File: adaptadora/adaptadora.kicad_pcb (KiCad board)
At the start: 2 copper layers, 193 x 100 mm, 106 parts, among them J1 Conn_Coaxial, J10 Conn_Coaxial, J11 Conn_Coaxial, J12 Conn_Coaxial, J13 Conn_Coaxial, J14 Conn_Coaxial, J15 Conn_Coaxial, J16 Conn_Coaxial, J17 Conn_Coaxial, J18 Conn_Coaxial, J19 Conn_Coaxial, J2 Conn_Coaxial, J20 Conn_Coaxial, J22 Conn_Coaxial, J3 Conn_Coaxial, J4 Conn_Coaxial, J5 Conn_02x20_Odd_Even, J6 Conn_01x02, J7 Conn_02x20_Odd_Even, J8 Conn_01x04, J9 Conn_01x02, U11 LM361MX_NOPB, U12 LM361MX_NOPB, U13 LM361MX_NOPB, U14 LM361MX_NOPB, U21 TLV2772IDR, U22 TLV2772IDR, U23 TLV2772IDR, U25 TLV2772IDR, U31 SN74LVC2T45DCUR, U32 SN74LVC2T45DCUR

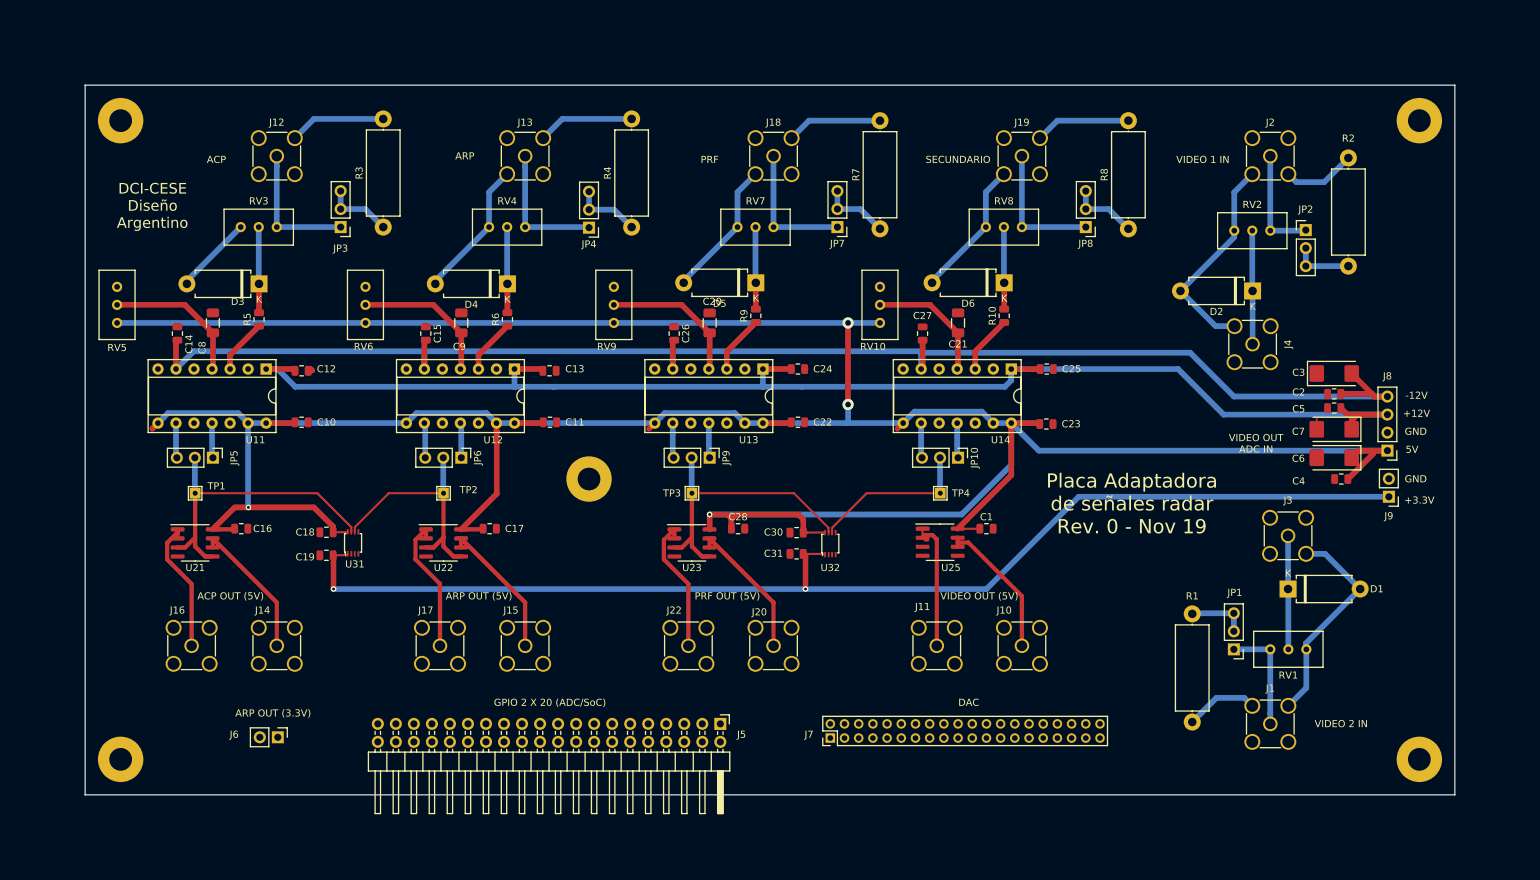
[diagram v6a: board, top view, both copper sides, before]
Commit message: se agrega planos de tierra
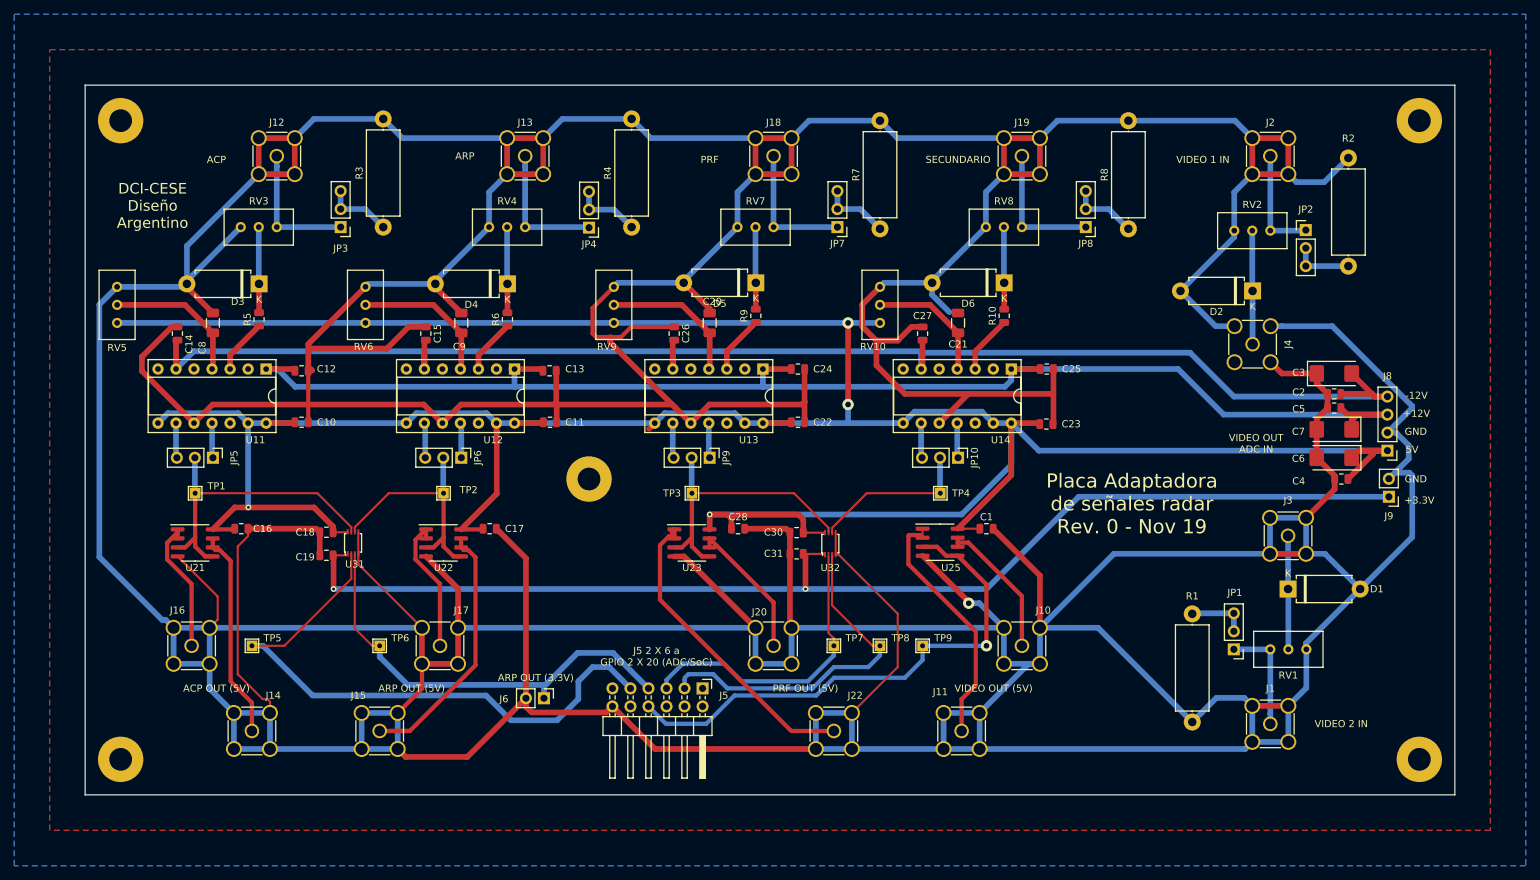
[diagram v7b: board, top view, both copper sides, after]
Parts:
- removed J7: Conn_02x20_Odd_Even, Connector_PinHeader_2.00mm:PinHeader_2x20_P2.00mm_Vertical
- added TP5: TestPoint, adaptadora:TestPoint_THTPad_1.5x1.5mm_Drill0.7mm, F.Cu at (67.5, 124.0)
- added TP6: TestPoint, adaptadora:TestPoint_THTPad_1.5x1.5mm_Drill0.7mm, F.Cu at (85.5, 124.0)
- added TP7: TestPoint, adaptadora:TestPoint_THTPad_1.5x1.5mm_Drill0.7mm, F.Cu at (149.5, 124.0)
- added TP8: TestPoint, adaptadora:TestPoint_THTPad_1.5x1.5mm_Drill0.7mm, F.Cu at (156.0, 124.0)
- added TP9: TestPoint, adaptadora:TestPoint_THTPad_1.5x1.5mm_Drill0.7mm, F.Cu at (162.0, 124.0)
- J5: value Conn_02x20_Odd_Even -> Conn_02x06_Odd_Even; footprint Connector_PinHeader_2.54mm:PinHeader_2x20_P2.54mm_Horizontal -> Connector_PinHeader_2.54mm:PinHeader_2x06_P2.54mm_Horizontal
- R10, R5, R6, R9: value 100-1/8W-5% -> 100 - 1/8W - 5%
- moved J6 37.9 mm to (108.7, 131.4)
- moved J15 23.8 mm to (85.5, 136.0)
- moved J22 23.8 mm to (149.5, 136.0)
- moved J11 12.5 mm to (167.5, 136.0)
- moved J14 12.5 mm to (67.5, 136.0)
- moved J5 5.59 mm to (131.0, 130.0)
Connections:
- J5 pad 1: /ACP_3P3 -> Net-(J5-Pad1)
- J5 pad 2: /VIDEO_DIGITAL -> Net-(J5-Pad2)
- J5 pad 3: /ACP_3P3 -> /V_COMP_3P3
- J5 pad 4: DAC_CLK -> Net-(J5-Pad4)
- J5 pad 7: /V_COMP_3P3 -> /ARP_3P3
- J5 pad 8: Net-(J5-Pad8) -> /VIDEO_DIGITAL
- J5 pad 9: Net-(J5-Pad9) -> /ACP_3P3
- J6 pad 1: /ACP_3P3 -> /ARP_3P3
- U31 pad 3: /ACP_3P3 -> /ARP_3P3
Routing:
- net GND: track 207.9 -> 1592.2 mm, vias 0 -> 1
- net /ACP_3P3: track 0.00 -> 84.9 mm
- net /VIDEO_DIGITAL: track 0.00 -> 74.2 mm, vias 0 -> 1
- net /ARP_3P3: track 0.00 -> 61.9 mm
- net /V_COMP_3P3: track 0.00 -> 50.3 mm
- net /PRF_3P3: track 0.00 -> 42.4 mm
- net Net-(J22-Pad1): track 19.7 -> 44.2 mm
- net Net-(J15-Pad1): track 20.1 -> 38.9 mm
- net Net-(J11-Pad1): track 19.6 -> 35.7 mm
- net Net-(J14-Pad1): track 19.9 -> 29.7 mm
- net +5V: track 484.8 -> 482.5 mm
- added copper zone on B.Cu, net GND
- added copper zone on F.Cu, net GND
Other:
- board text added: "J5 2 X 6 a GPIO 2 X 20 (ADC/SoC)"
- board text removed: "DAC"
- board text removed: "GPIO 2 X 20 (ADC/SoC)"
